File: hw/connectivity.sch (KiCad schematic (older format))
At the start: 127 parts, among them P1 CONN_13X3, P10 MICROSD, P11 CONN_9, P12 CONN_2, P13 CONN_6, P19 CONN_1, P2 CONN_4, P20 CONN_1, P21 CONN_1, P22 CONN_1, P3 CONN_4, P4 MICROUSB, P5 CONN_4, P6 CONN_6, P7 CONN_4, P8 CONN_4, P9 CONN_4, Q1 NTA4153NT1G, Q2 NTA4153NT1G, Q3 NTA4151PT1G, Q4 PDTC114EE, Q5 PDTC114EE, Q6 PDTC114EE, Q7 PDTC114EE, SW1 STG719, U1 XBEE, U12 MAX4090, U2 LTC4411, U3 SN65HVD233, U4 ADP3338AKCZ-3.3, U5 LT1761-3.3, U6 EL1883

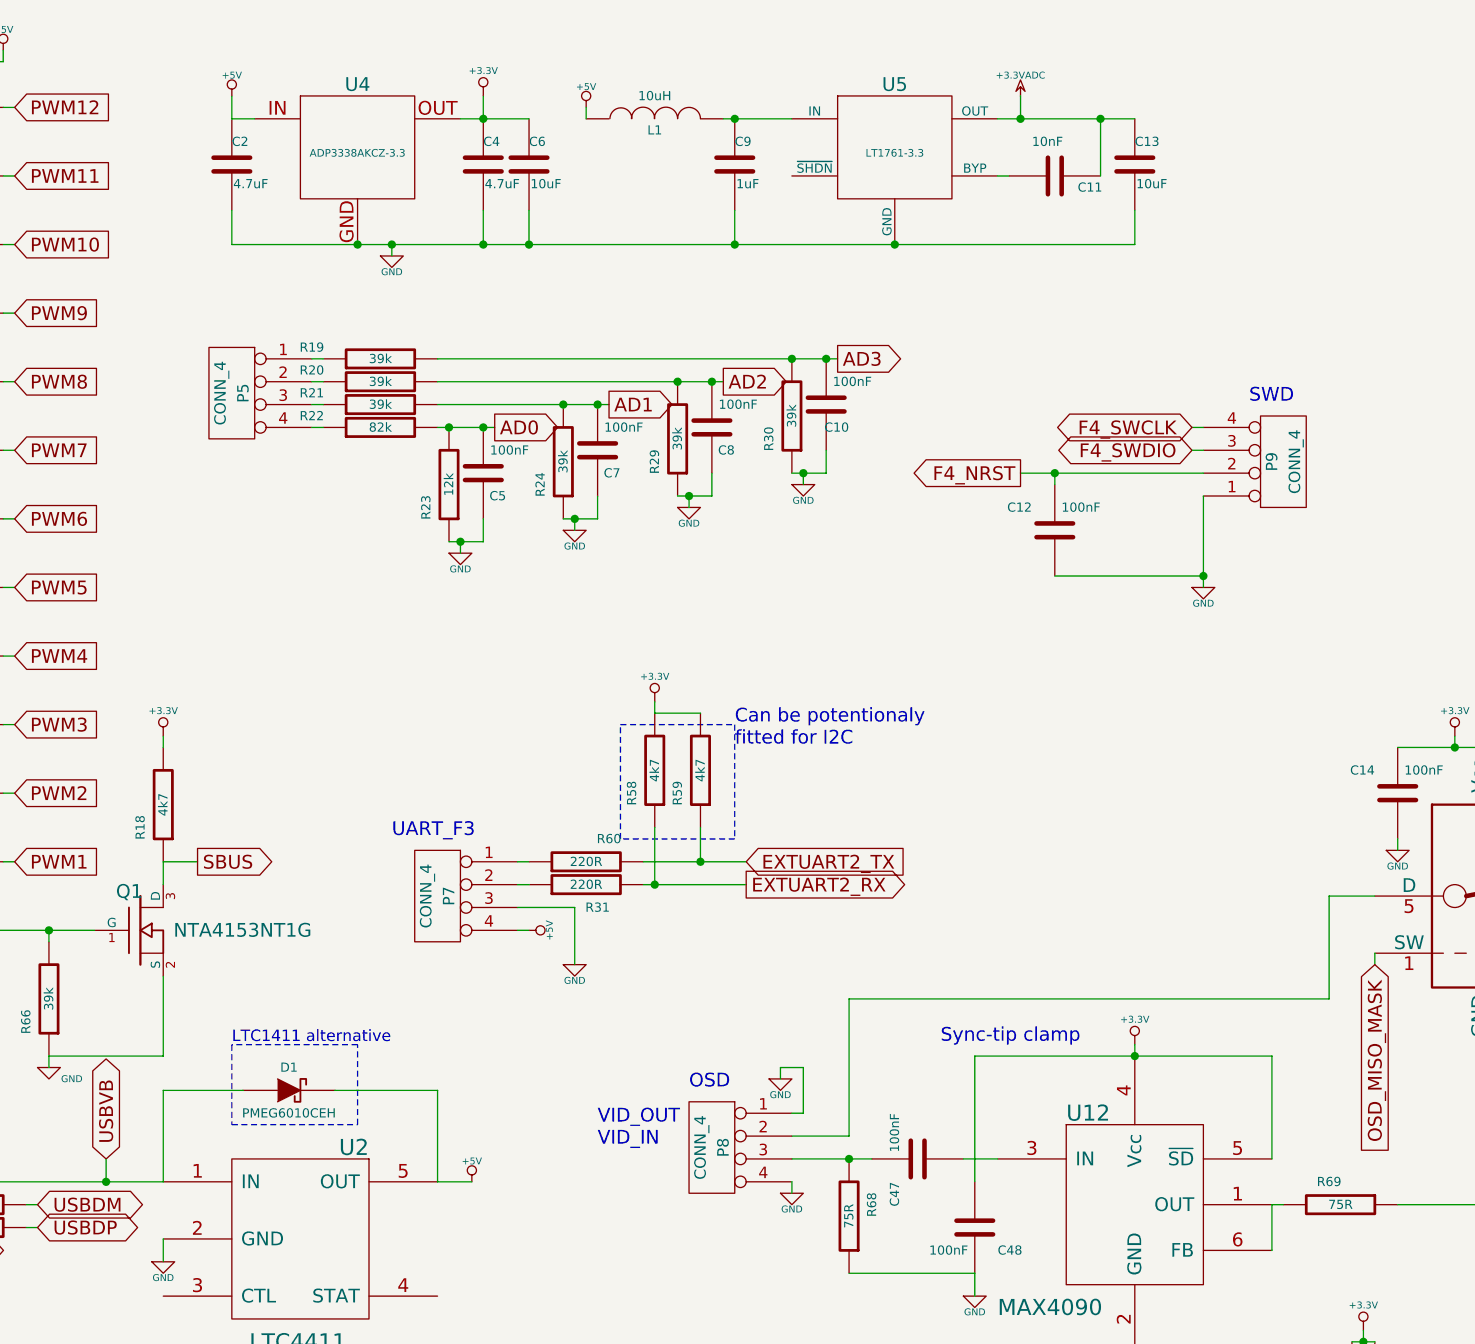
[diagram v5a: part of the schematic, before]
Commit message: hw: added diode from servo +5V to +3.3V stabs, TSV protection diode
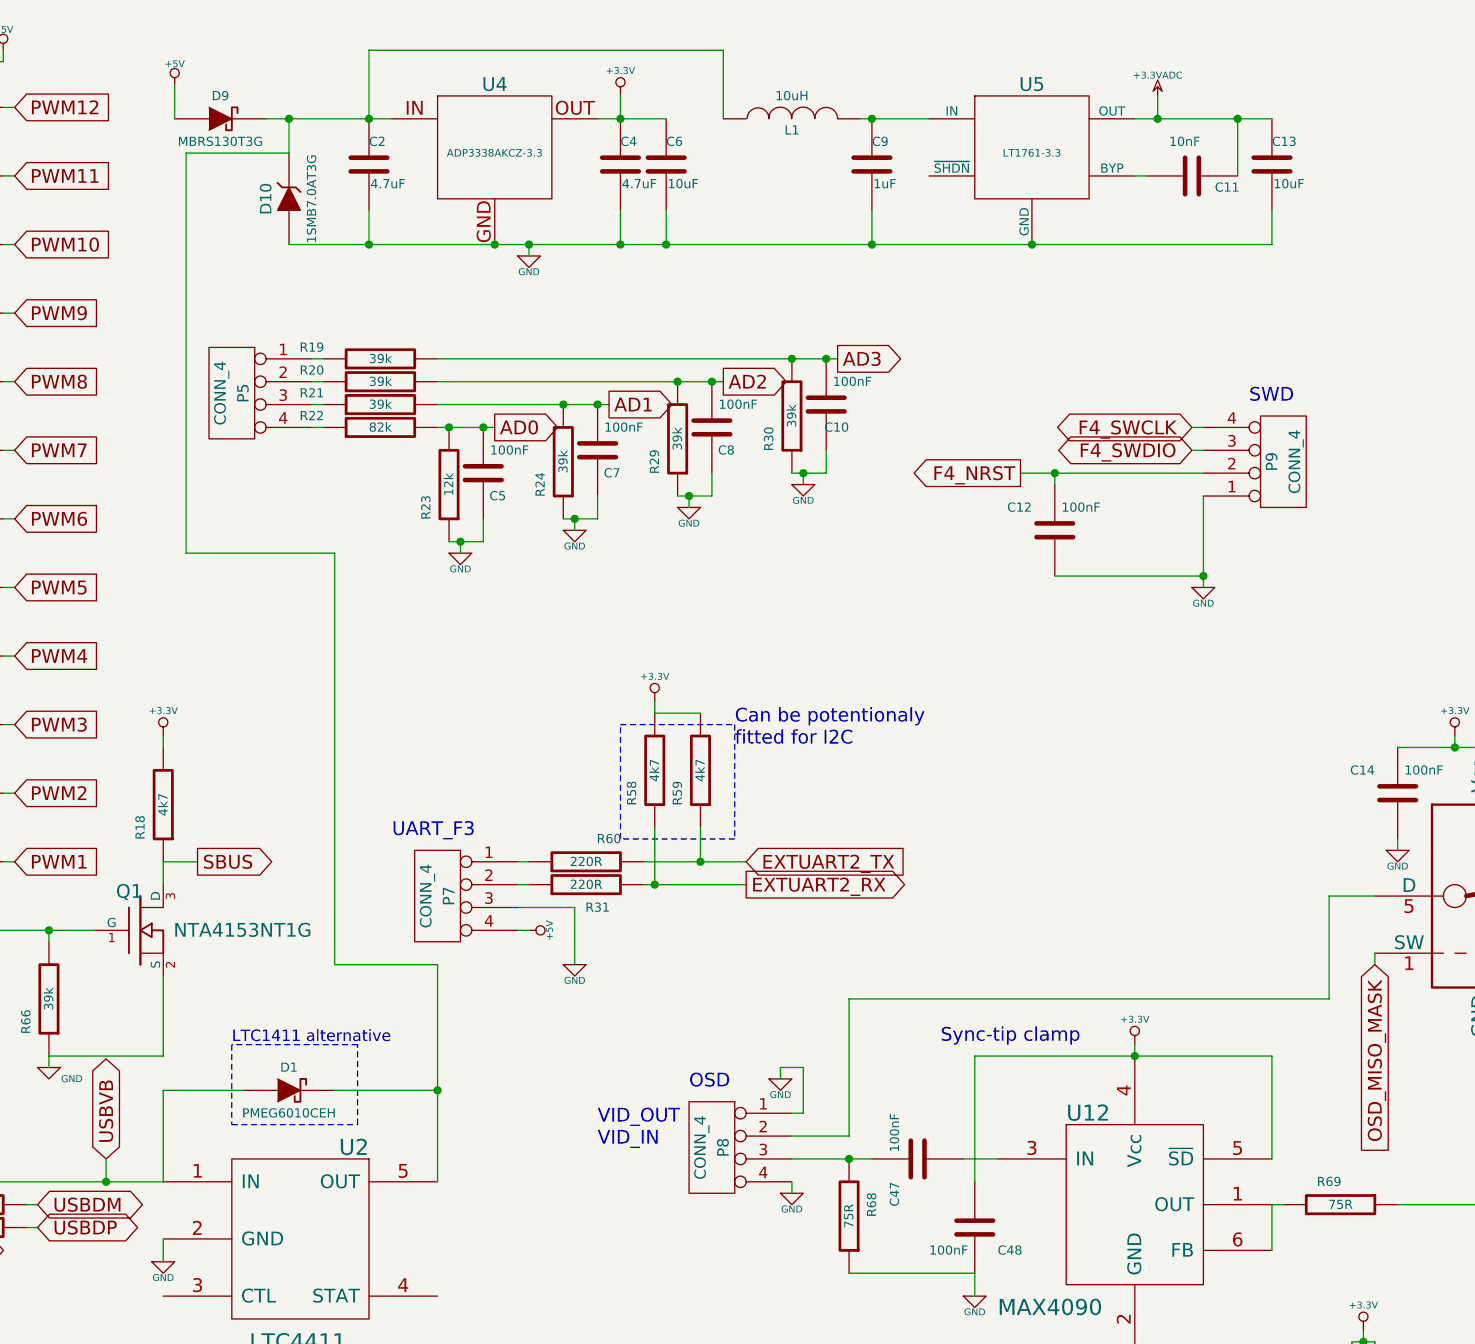
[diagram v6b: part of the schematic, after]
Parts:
- added D10: 1SMB7.0AT3G, ~, symbol ZENER
- added D9: MBRS130T3G, ~, symbol DIODESCH
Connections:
- wire segments 315 -> 322
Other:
- moved on the sheet: C11, C13, C2, C4, C6, C9, L1, U4, U5

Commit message: hw: SBUS inverting FET replaced by XOR gate (controllable inverter)
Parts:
- removed Q1: NTA4153NT1G, ~, symbol NTA4153NT1G
- removed R18: 4k7, r_0603, symbol R
- added C43: 100nF, c_0603, symbol C
- added U11: SN74AHC1G86, ~, symbol SN74AHC1G86
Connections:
- net labels added: SBUS_UART_INVERT
- wire segments 322 -> 324
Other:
- moved on the sheet: R66

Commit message: hw: added series resistor to USB VBUS sense pin
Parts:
- added R18: 39k, r_0603, symbol R
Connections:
- wire segments 324 -> 325
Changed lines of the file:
@@
 Sheet 2 3
 Title "DRACO - connectivity sheet"
-Date "24 sep 2014"
+Date "25 sep 2014"
 Rev "1.1"
 Comp "dandys"
@@
 Wire Wire Line
 	1450 5800 1500 5800
-Text GLabel 2200 5500 1    60   BiDi ~ 0
+Text GLabel 2050 5450 2    60   BiDi ~ 0
 USBVB
 $Comp
@@
 Wire Wire Line
 	2450 5100 2450 5200
+$Comp
+L R R18
+U 1 1 54242744
+P 1750 5450
+F 0 "R18" V 1850 5550 40  0000 C CNN
+F 1 "39k" V 1750 5450 40  0000 C CNN
+F 2 "r_0603" V 1680 5450 30  0001 C CNN
+F 3 "~" H 1750 5450 30  0000 C CNN
+	1    1750 5450
+	0    1    1    0
+$EndComp
+Wire Wire Line
+	2000 5450 2050 5450
 Wire Wire Line
-	2200 5500 2200 5600
-Connection ~ 2200 5600
+	1500 5450 1500 5600
+Connection ~ 1500 5600
 $EndSCHEMATC
